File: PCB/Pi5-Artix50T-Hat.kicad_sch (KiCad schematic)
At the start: 0 parts

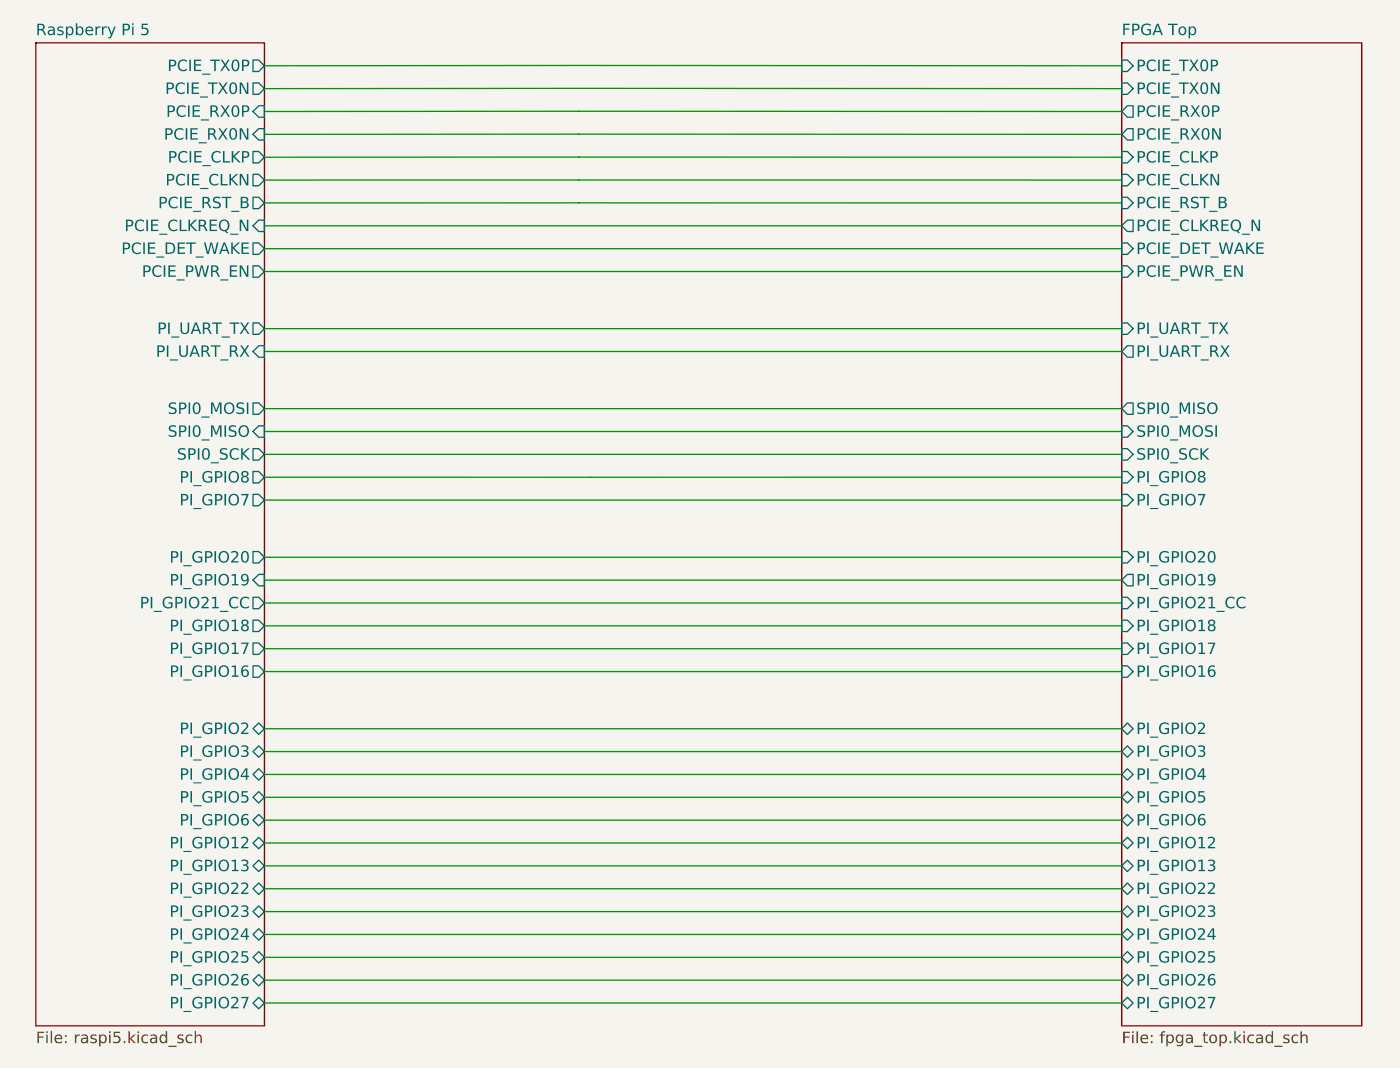
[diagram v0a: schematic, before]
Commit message: Updated PCB to remove MOSI-MISO cross. Updated texts. New images.
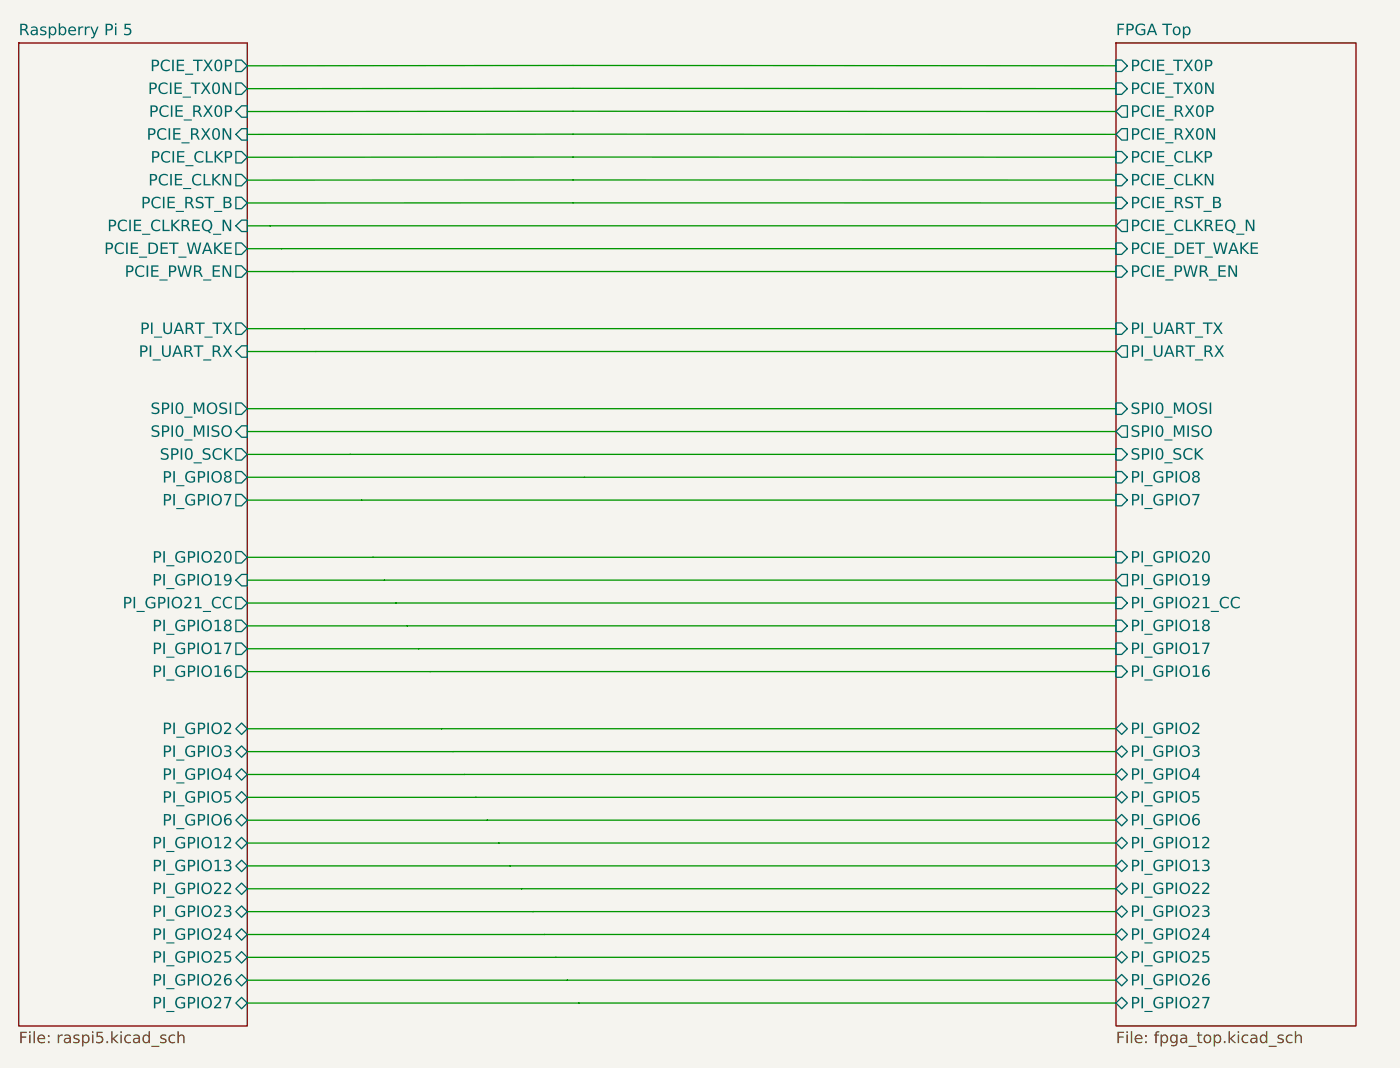
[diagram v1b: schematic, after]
